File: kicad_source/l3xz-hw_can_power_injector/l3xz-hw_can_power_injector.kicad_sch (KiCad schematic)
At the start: 44 parts, among them CN1 DNI, CN2 SM04B-GHS-TB, CN3 SM04B-GHS-TB, CN4 Conn_01x02, CN5 SM04B-GHS-TB, CN6 SM04B-GHS-TB, CN7 DNI, U1 RAA211650

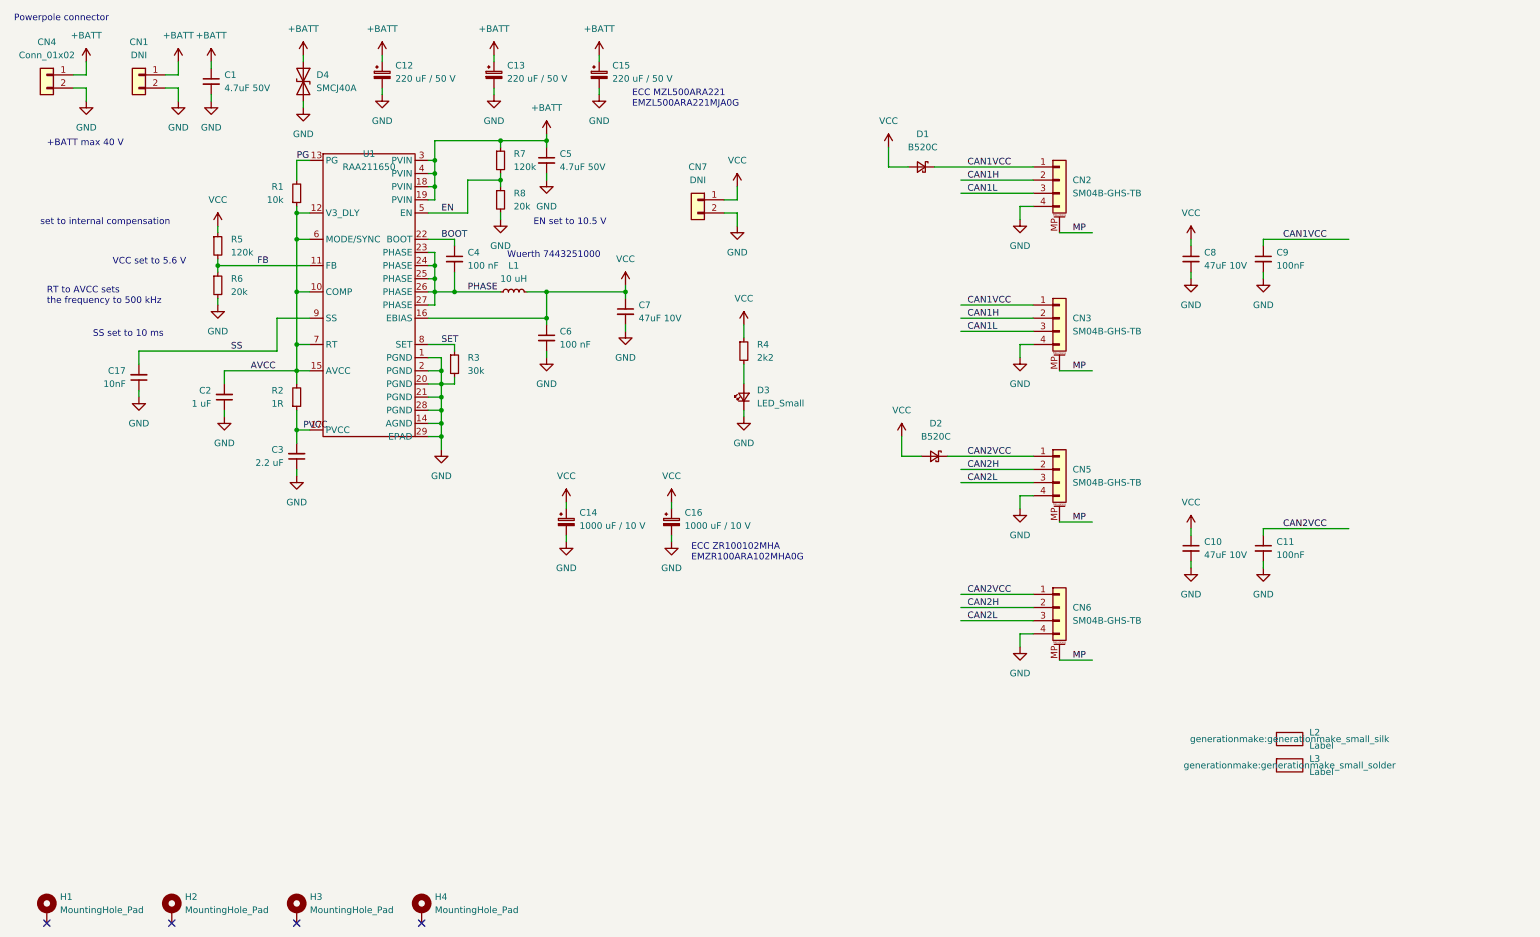
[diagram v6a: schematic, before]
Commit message: added some texts to pcb, generated BOM, updated schemtatic pdf
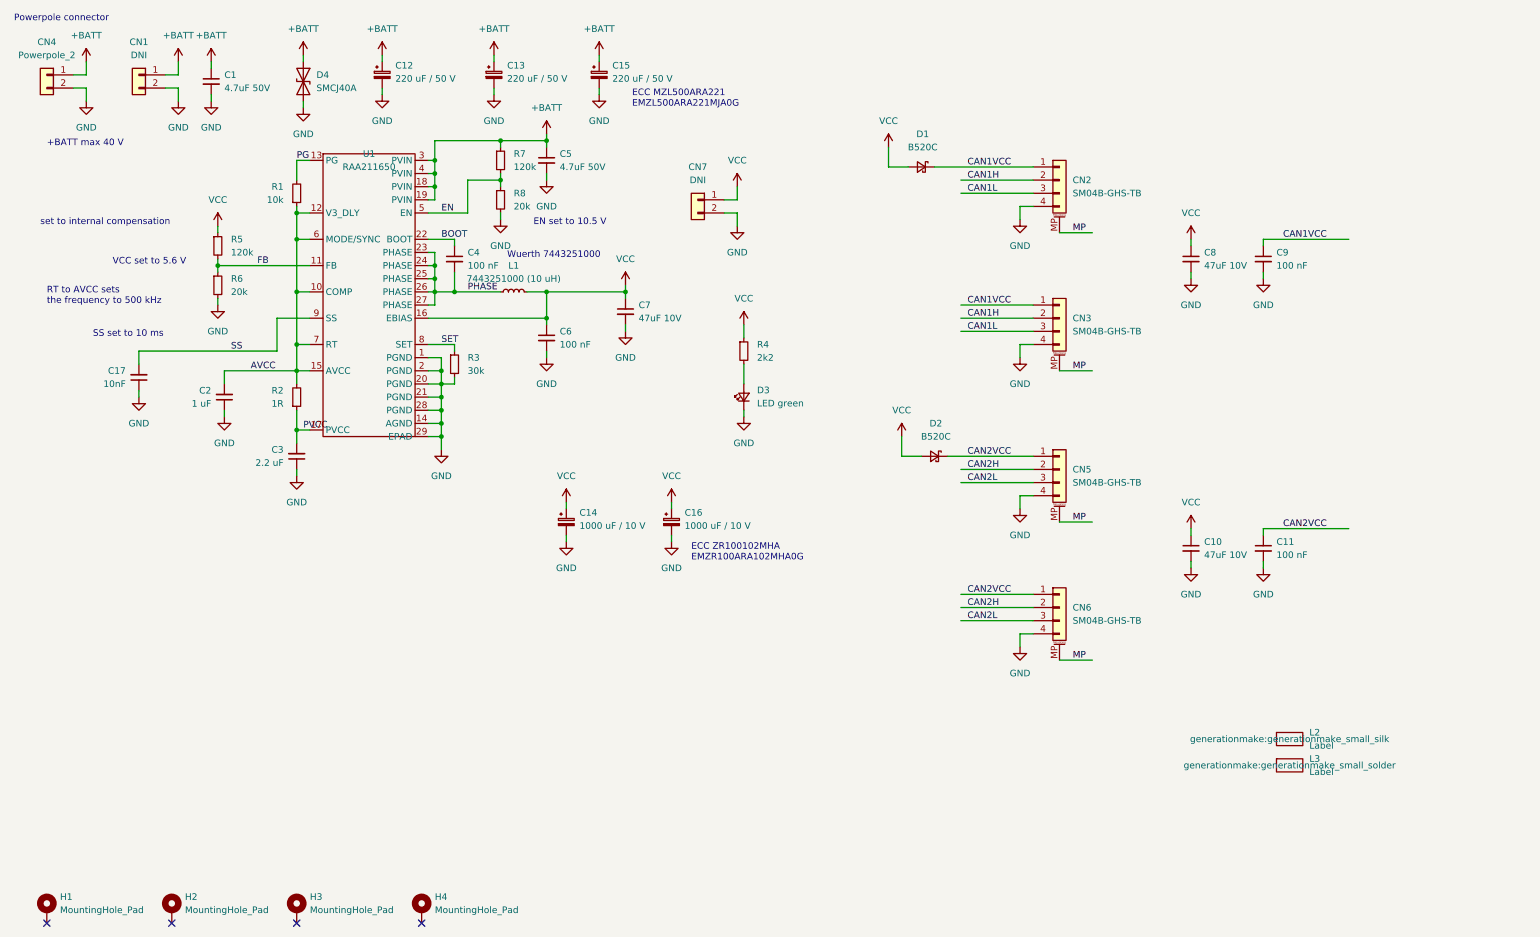
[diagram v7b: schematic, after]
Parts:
- C11, C9: value 100nF -> 100 nF
- CN4: value Conn_01x02 -> Powerpole_2
- D3: value LED_Small -> LED green
- H1, H2, H3, H4, L2, L3: now left out of the parts list
- L1: value 10 uH -> 7443251000 (10 uH)
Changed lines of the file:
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@@
   (title_block
     (title "l3xz-hw_can_power_injector")
-    (date "2022-11-06")
+    (date "2022-11-30")
     (rev "0.1")
     (company "107-systems")
@@
   )
   (symbol (lib_id "generationmake:Label") (at 261.62 156.21 0) (unit 1)
-    (in_bom yes) (on_board yes) (fields_autoplaced)
+    (in_bom no) (on_board yes) (fields_autoplaced)
     (property "Reference" "L2" (id 0) (at 265.43 154.9399 0)
       (effects (font (size 1.27 1.27)) (justify left))
@@
   )
   (symbol (lib_id "Mechanical:MountingHole_Pad") (at 21.59 189.23 0) (unit 1)
-    (in_bom yes) (on_board yes) (fields_autoplaced)
+    (in_bom no) (on_board yes) (fields_autoplaced)
     (property "Reference" "H1" (id 0) (at 24.13 186.6899 0)
       (effects (font (size 1.27 1.27)) (justify left))
@@
       (effects (font (size 1.27 1.27)) (justify right))
     )
-    (property "Value" "LED_Small" (id 1) (at 158.75 91.3764 90)
+    (property "Value" "LED green" (id 1) (at 158.75 91.3764 90)
       (effects (font (size 1.27 1.27)) (justify right))
     )
@@
     (in_bom yes) (on_board yes) (fields_autoplaced)
     (property "Reference" "L1" (id 0) (at 111.76 64.77 90))
-    (property "Value" "10 uH" (id 1) (at 111.76 67.31 90))
+    (property "Value" "7443251000 (10 uH)" (id 1) (at 111.76 67.31 90))
     (property "Footprint" "Inductor_SMD:L_Wuerth_HCI-1050" (id 2) (at 111.76 69.85 0)
       (effects (font (size 1.27 1.27)) hide)
@@
       (effects (font (size 1.27 1.27)) (justify left))
     )
-    (property "Value" "100nF" (id 1) (at 259.08 64.7762 0)
+    (property "Value" "100 nF" (id 1) (at 259.08 64.7762 0)
       (effects (font (size 1.27 1.27)) (justify left))
     )
@@
   )
   (symbol (lib_id "Mechanical:MountingHole_Pad") (at 93.98 189.23 0) (unit 1)
-    (in_bom yes) (on_board yes) (fields_autoplaced)
+    (in_bom no) (on_board yes) (fields_autoplaced)
     (property "Reference" "H4" (id 0) (at 96.52 186.6899 0)
       (effects (font (size 1.27 1.27)) (justify left))
@@
       (effects (font (size 1.27 1.27)) (justify left))
     )
-    (property "Value" "100nF" (id 1) (at 259.08 120.6562 0)
+    (property "Value" "100 nF" (id 1) (at 259.08 120.6562 0)
       (effects (font (size 1.27 1.27)) (justify left))
     )
@@
     (in_bom yes) (on_board yes) (fields_autoplaced)
     (property "Reference" "CN4" (id 0) (at 21.59 21.59 0))
-    (property "Value" "Conn_01x02" (id 1) (at 21.59 24.13 0))
+    (property "Value" "Powerpole_2" (id 1) (at 21.59 24.13 0))
     (property "Footprint" "generationmake:POWERPOLE_hor_2" (id 2) (at 21.59 27.94 0)
       (effects (font (size 1.27 1.27)) hide)
@@
   )
   (symbol (lib_id "Mechanical:MountingHole_Pad") (at 69.85 189.23 0) (unit 1)
-    (in_bom yes) (on_board yes) (fields_autoplaced)
+    (in_bom no) (on_board yes) (fields_autoplaced)
     (property "Reference" "H3" (id 0) (at 72.39 186.6899 0)
       (effects (font (size 1.27 1.27)) (justify left))
@@
   )
   (symbol (lib_id "generationmake:Label") (at 261.62 161.29 0) (unit 1)
-    (in_bom yes) (on_board yes) (fields_autoplaced)
+    (in_bom no) (on_board yes) (fields_autoplaced)
     (property "Reference" "L3" (id 0) (at 265.43 160.0199 0)
       (effects (font (size 1.27 1.27)) (justify left))
@@
   )
   (symbol (lib_id "Mechanical:MountingHole_Pad") (at 45.72 189.23 0) (unit 1)
-    (in_bom yes) (on_board yes) (fields_autoplaced)
+    (in_bom no) (on_board yes) (fields_autoplaced)
     (property "Reference" "H2" (id 0) (at 48.26 186.6899 0)
       (effects (font (size 1.27 1.27)) (justify left))
@@
     )
     (path "/40fd1244-d027-4abc-a17d-3da295028d0c"
-      (reference "C9") (unit 1) (value "100nF") (footprint "Capacitor_SMD:C_0603_1608Metric")
+      (reference "C9") (unit 1) (value "100 nF") (footprint "Capacitor_SMD:C_0603_1608Metric")
     )
     (path "/4b87a511-f1ff-403b-82bb-48a1b6d84d3c"
@@
     )
     (path "/8263f46b-91e2-4edf-a9b1-dab669402431"
-      (reference "C11") (unit 1) (value "100nF") (footprint "Capacitor_SMD:C_0603_1608Metric")
+      (reference "C11") (unit 1) (value "100 nF") (footprint "Capacitor_SMD:C_0603_1608Metric")
     )
     (path "/8150ddc6-6836-42ce-9cdd-33fbb4f9853f"
@@
     )
     (path "/8a3827e6-26b6-4873-9005-56e501165c36"
-      (reference "CN4") (unit 1) (value "Conn_01x02") (footprint "generationmake:POWERPOLE_hor_2")
+      (reference "CN4") (unit 1) (value "Powerpole_2") (footprint "generationmake:POWERPOLE_hor_2")
     )
     (path "/376c86d1-5d77-4c61-a230-7bb0b699818d"
@@
     )
     (path "/2cb2d04c-0cc5-487d-8f84-20c79a27fb91"
-      (reference "D3") (unit 1) (value "LED_Small") (footprint "LED_SMD:LED_0603_1608Metric")
+      (reference "D3") (unit 1) (value "LED green") (footprint "LED_SMD:LED_0603_1608Metric")
     )
     (path "/a419651c-7676-4edd-aef0-649ff3d3b0c4"
@@
     )
     (path "/2f54f438-5d34-4db6-a425-bb6ed0e0f809"
-      (reference "L1") (unit 1) (value "10 uH") (footprint "Inductor_SMD:L_Wuerth_HCI-1050")
+      (reference "L1") (unit 1) (value "7443251000 (10 uH)") (footprint "Inductor_SMD:L_Wuerth_HCI-1050")
     )
     (path "/03c2a0ad-6922-4fa5-9a56-bcd869881ef1"

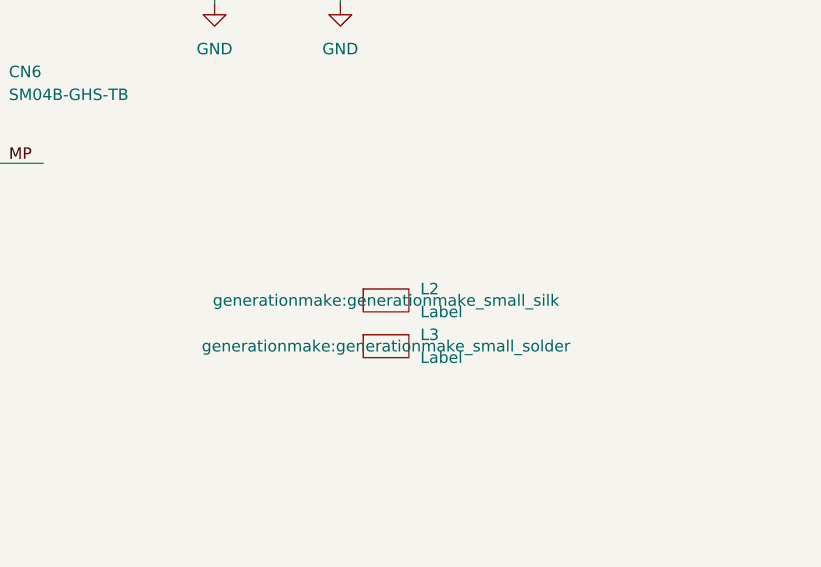
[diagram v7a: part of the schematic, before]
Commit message: added some labels
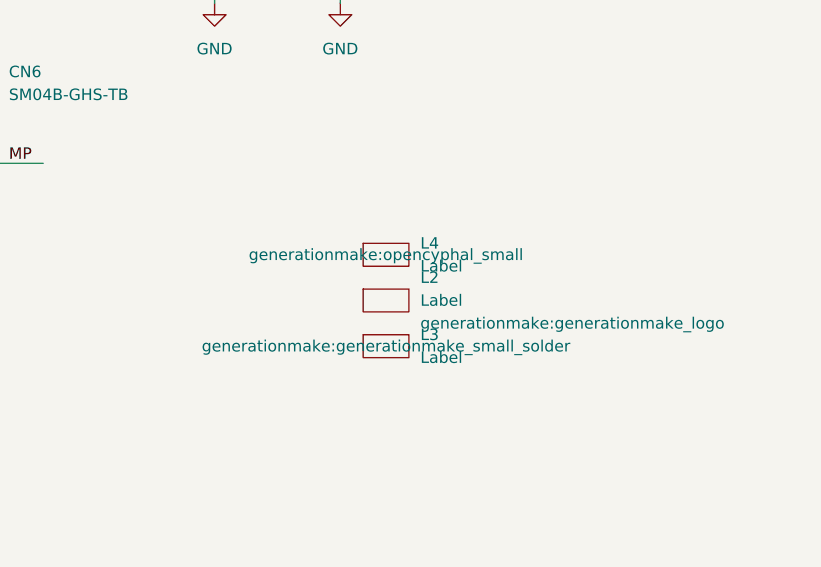
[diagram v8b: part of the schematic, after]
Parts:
- added L4: Label, generationmake:opencyphal_small, symbol generationmake:Label
- L2: footprint generationmake:generationmake_small_silk -> generationmake:generationmake_logo
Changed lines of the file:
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@@
   (symbol (lib_id "generationmake:Label") (at 261.62 156.21 0) (unit 1)
     (in_bom no) (on_board yes) (fields_autoplaced)
-    (property "Reference" "L2" (id 0) (at 265.43 154.9399 0)
-      (effects (font (size 1.27 1.27)) (justify left))
-    )
-    (property "Value" "Label" (id 1) (at 265.43 157.4799 0)
-      (effects (font (size 1.27 1.27)) (justify left))
-    )
-    (property "Footprint" "generationmake:generationmake_small_silk" (id 2) (at 261.62 156.21 0))
+    (property "Reference" "L2" (id 0) (at 265.43 153.6699 0)
+      (effects (font (size 1.27 1.27)) (justify left))
+    )
+    (property "Value" "Label" (id 1) (at 265.43 156.2099 0)
+      (effects (font (size 1.27 1.27)) (justify left))
+    )
+    (property "Footprint" "generationmake:generationmake_logo" (id 2) (at 265.43 158.7499 0)
+      (effects (font (size 1.27 1.27)) (justify left))
+    )
     (property "Datasheet" "" (id 3) (at 261.62 156.21 0)
       (effects (font (size 1.27 1.27)) hide)
@@
     (pin "2")
   )
+  (symbol (lib_id "generationmake:Label") (at 261.62 151.13 0) (unit 1)
+    (in_bom no) (on_board yes) (fields_autoplaced)
+    (property "Reference" "L4" (id 0) (at 265.43 149.8599 0)
+      (effects (font (size 1.27 1.27)) (justify left))
+    )
+    (property "Value" "Label" (id 1) (at 265.43 152.3999 0)
+      (effects (font (size 1.27 1.27)) (justify left))
+    )
+    (property "Footprint" "generationmake:opencyphal_small" (id 2) (at 261.62 151.13 0))
+    (property "Datasheet" "" (id 3) (at 261.62 151.13 0)
+      (effects (font (size 1.27 1.27)) hide)
+    )
+  )
   (symbol (lib_id "power:VCC") (at 121.92 110.49 0) (unit 1)
     (in_bom yes) (on_board yes) (fields_autoplaced)
@@
     )
     (path "/03c2a0ad-6922-4fa5-9a56-bcd869881ef1"
-      (reference "L2") (unit 1) (value "Label") (footprint "generationmake:generationmake_small_silk")
+      (reference "L2") (unit 1) (value "Label") (footprint "generationmake:generationmake_logo")
     )
     (path "/d082734d-ae95-481b-9a5f-c2add0f0313d"
       (reference "L3") (unit 1) (value "Label") (footprint "generationmake:generationmake_small_solder")
     )
+    (path "/c7020686-eb6c-4c08-8fbd-604b14b93f59"
+      (reference "L4") (unit 1) (value "Label") (footprint "generationmake:opencyphal_small")
+    )
     (path "/a366e47f-47b8-4224-93d4-b15e91e768de"
